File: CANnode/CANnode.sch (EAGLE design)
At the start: 247 parts, among them IC1 ISO1050DUB, IC2 ISO1050DUB, Q1 FDV302P, Q3 FDV302P, U1 LM324PW, U10 FT2232HL, U11 93LC56C-I/SN, U2 TPS70445_PWP_24, U3 LM324PW, U4 LM324PW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

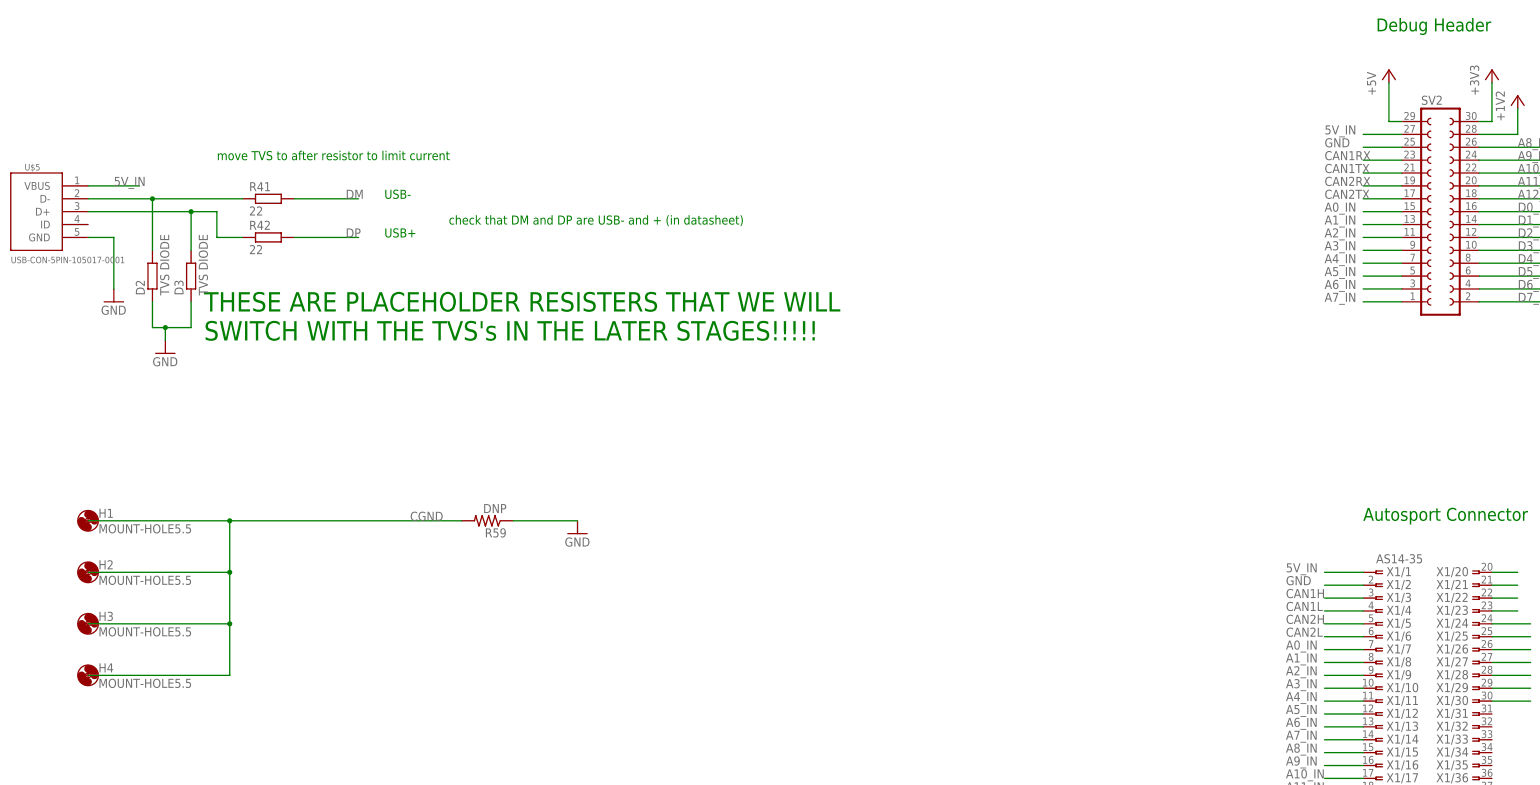
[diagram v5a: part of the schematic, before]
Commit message: Changed mounting holes to big vias. Move the origin of the board.
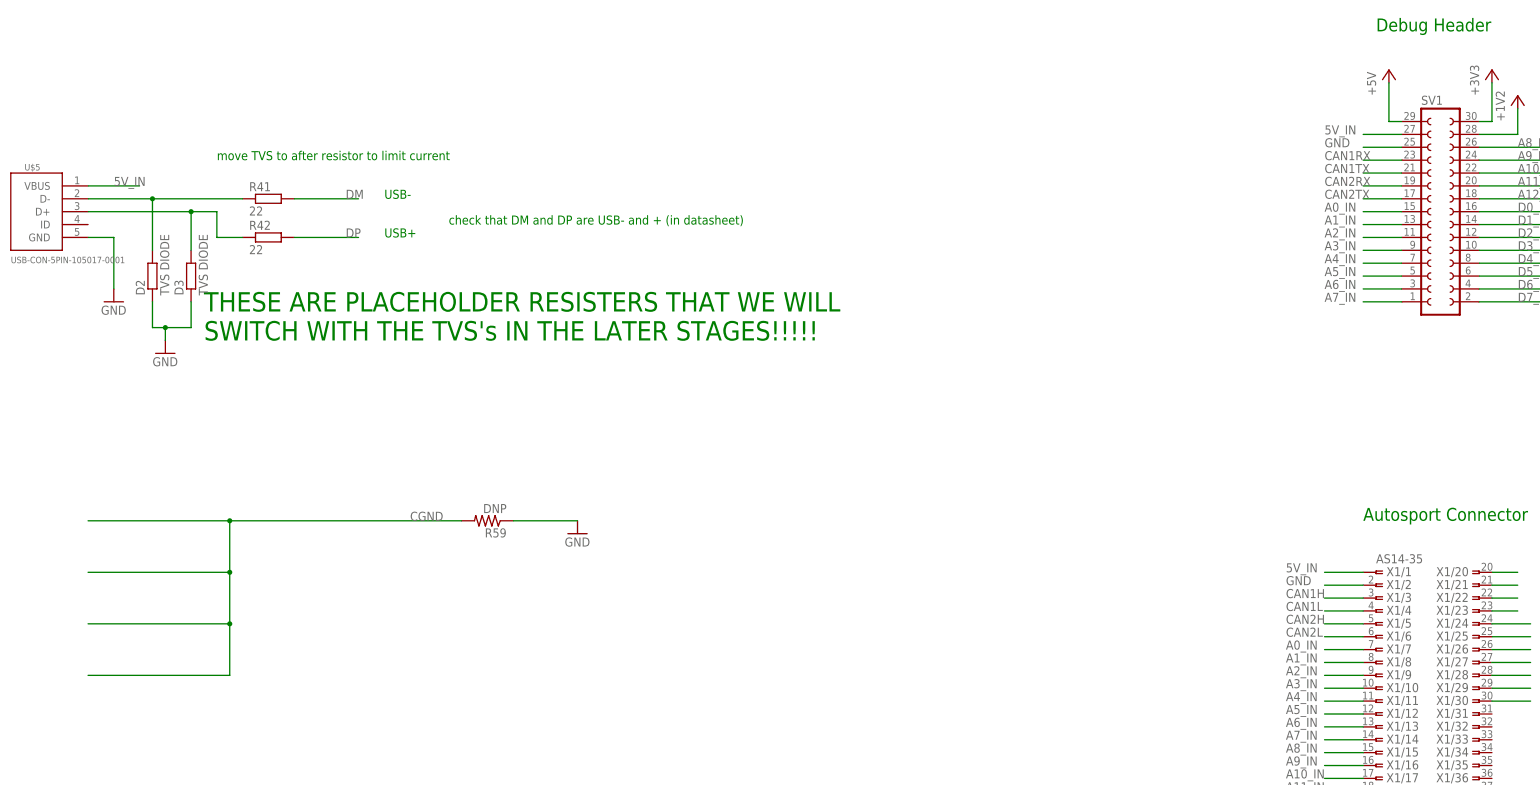
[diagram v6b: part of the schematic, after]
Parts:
- removed H1, H2, H3, H4: MOUNT-HOLE5.5, holes:MOUNT-HOLE5.5
- renumbered SV2 to SV1
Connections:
- net 5V_IN: now also SV1.27
- net A0_IN: now also SV1.15
- net A10_IN: now also SV1.22
- net A11_IN: now also SV1.20
- net A12_IN: now also SV1.18
- net A1_IN: now also SV1.13
- net A2_IN: now also SV1.11
- net A3_IN: now also SV1.9
- net A4_IN: now also SV1.7
- net A5_IN: now also SV1.5
- net A6_IN: now also SV1.3
- net A8_IN: now also SV1.26
- net A9_IN: now also SV1.24
- net CAN1RX: now also SV1.23
- net CAN1TX: now also SV1.21
- net CAN2RX: now also SV1.19
- net CAN2TX: now also SV1.17
- net D0_IN: now also SV1.16
- net D1_IN: now also SV1.14
- net D2_IN: now also SV1.12
- net D3_IN: now also SV1.10
- net D4_IN: now also SV1.8
- net D5_IN: now also SV1.6
- net D6_IN: now also SV1.4
- net GND: now also SV1.25
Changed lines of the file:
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@@
 <part name="GND8" library="supply1" deviceset="GND" device=""/>
 <part name="TP1" library="testpad" deviceset="TPS" device="B1,27"/>
-<part name="SV2" library="con-lsta" deviceset="FE15-2" device=""/>
 <part name="P+4" library="supply1" deviceset="+5V" device=""/>
 <part name="+3V10" library="supply1" deviceset="+3V3" device=""/>
@@
 <part name="D34" library="eagle-ltspice" deviceset="R" device="R0402" value="TVS DIODE"/>
 <part name="D35" library="eagle-ltspice" deviceset="R" device="R0402" value="TVS DIODE"/>
-<part name="H1" library="holes" deviceset="MOUNT-HOLE" device="5.5"/>
-<part name="H2" library="holes" deviceset="MOUNT-HOLE" device="5.5"/>
-<part name="H3" library="holes" deviceset="MOUNT-HOLE" device="5.5"/>
-<part name="H4" library="holes" deviceset="MOUNT-HOLE" device="5.5"/>
 <part name="R59" library="resistor" deviceset="R-US_" device="R0402" value="DNP"/>
 <part name="GND120" library="supply1" deviceset="GND" device=""/>
@@
 <part name="GND123" library="supply1" deviceset="GND" device=""/>
 <part name="F1" library="adafruit" deviceset="PTCFUSE" device="-1206" value="0ZCJ0050AF2E"/>
+<part name="SV1" library="con-lsta" deviceset="FE15-2" device=""/>
 </parts>
 <sheets>
@@
 <instance part="GND8" gate="1" x="50.8" y="-5.08"/>
 <instance part="TP1" gate="G$1" x="116.84" y="-30.48"/>
-<instance part="SV2" gate="1" x="264.16" y="-83.82"/>
 <instance part="P+4" gate="1" x="254" y="-55.88"/>
 <instance part="+3V10" gate="G$1" x="274.32" y="-55.88"/>
@@
 <instance part="D34" gate="G$1" x="657.86" y="-314.96" rot="R90"/>
 <instance part="D35" gate="G$1" x="662.94" y="-360.68" rot="R90"/>
-<instance part="H1" gate="G$1" x="-2.54" y="-144.78"/>
-<instance part="H2" gate="G$1" x="-2.54" y="-154.94"/>
-<instance part="H3" gate="G$1" x="-2.54" y="-165.1"/>
-<instance part="H4" gate="G$1" x="-2.54" y="-175.26"/>
 <instance part="R59" gate="G$1" x="76.2" y="-144.78" rot="R180"/>
 <instance part="GND120" gate="1" x="93.98" y="-147.32"/>
@@
 <instance part="GND123" gate="1" x="58.42" y="-5.08"/>
 <instance part="F1" gate="G$1" x="15.24" y="10.16"/>
+<instance part="SV1" gate="1" x="264.16" y="-83.82"/>
 </instances>
 <busses>
@@
 <pinref part="+3V10" gate="G$1" pin="+3V3"/>
 <wire x1="274.32" y1="-58.42" x2="274.32" y2="-66.04" width="0.1524" layer="91"/>
-<pinref part="SV2" gate="1" pin="30"/>
 <wire x1="274.32" y1="-66.04" x2="271.78" y2="-66.04" width="0.1524" layer="91"/>
+<pinref part="SV1" gate="1" pin="30"/>
 </segment>
 <segment>
@@
 </segment>
 <segment>
-<pinref part="SV2" gate="1" pin="28"/>
 <wire x1="271.78" y1="-68.58" x2="279.4" y2="-68.58" width="0.1524" layer="91"/>
 <wire x1="279.4" y1="-68.58" x2="279.4" y2="-63.5" width="0.1524" layer="91"/>
 <pinref part="U$2" gate="A" pin="+1V2"/>
+<pinref part="SV1" gate="1" pin="28"/>
 </segment>
 </net>
@@
 <wire x1="256.54" y1="-76.2" x2="248.92" y2="-76.2" width="0.1524" layer="91"/>
 <label x="241.3" y="-76.2" size="1.778" layer="95"/>
+<pinref part="SV1" gate="1" pin="21"/>
 </segment>
 </net>
@@
 <wire x1="256.54" y1="-81.28" x2="248.92" y2="-81.28" width="0.1524" layer="91"/>
 <label x="241.3" y="-81.28" size="1.778" layer="95"/>
+<pinref part="SV1" gate="1" pin="17"/>
 </segment>
 </net>
@@
 <wire x1="248.92" y1="-78.74" x2="256.54" y2="-78.74" width="0.1524" layer="91"/>
 <label x="241.3" y="-78.74" size="1.778" layer="95"/>
+<pinref part="SV1" gate="1" pin="19"/>
 </segment>
 </net>
@@
 <wire x1="256.54" y1="-73.66" x2="248.92" y2="-73.66" width="0.1524" layer="91"/>
 <label x="241.3" y="-73.66" size="1.778" layer="95"/>
+<pinref part="SV1" gate="1" pin="23"/>
 </segment>
 </net>
@@
 <wire x1="256.54" y1="-71.12" x2="248.92" y2="-71.12" width="0.1524" layer="91"/>
 <label x="241.3" y="-71.12" size="1.778" layer="95"/>
+<pinref part="SV1" gate="1" pin="25"/>
 </segment>
 <segment>
@@
 <wire x1="256.54" y1="-68.58" x2="248.92" y2="-68.58" width="0.1524" layer="91"/>
 <label x="241.3" y="-68.58" size="1.778" layer="95"/>
+<pinref part="SV1" gate="1" pin="27"/>
 </segment>
 <segment>
@@
 <net name="+5V" class="0">
 <segment>
-<pinref part="SV2" gate="1" pin="29"/>
 <wire x1="256.54" y1="-66.04" x2="254" y2="-66.04" width="0.1524" layer="91"/>
 <pinref part="P+4" gate="1" pin="+5V"/>
 <wire x1="254" y1="-66.04" x2="254" y2="-58.42" width="0.1524" layer="91"/>
+<pinref part="SV1" gate="1" pin="29"/>
 </segment>
 <segment>
@@
 <label x="241.3" y="-83.82" size="1.778" layer="95"/>
 <wire x1="248.92" y1="-83.82" x2="256.54" y2="-83.82" width="0.1524" layer="91"/>
+<pinref part="SV1" gate="1" pin="15"/>
 </segment>
 </net>
@@
 <label x="241.3" y="-93.98" size="1.778" layer="95"/>
 <wire x1="248.92" y1="-93.98" x2="256.54" y2="-93.98" width="0.1524" layer="91"/>
+<pinref part="SV1" gate="1" pin="7"/>
 </segment>
 </net>
@@
 <label x="279.4" y="-71.12" size="1.778" layer="95"/>
 <wire x1="271.78" y1="-71.12" x2="287.02" y2="-71.12" width="0.1524" layer="91"/>
+<pinref part="SV1" gate="1" pin="26"/>
 </segment>
 </net>
@@
 <label x="279.4" y="-81.28" size="1.778" layer="95"/>
 <wire x1="271.78" y1="-81.28" x2="287.02" y2="-81.28" width="0.1524" layer="91"/>
+<pinref part="SV1" gate="1" pin="18"/>
 </segment>
 </net>
@@
 <label x="279.4" y="-83.82" size="1.778" layer="95"/>
 <wire x1="271.78" y1="-83.82" x2="287.02" y2="-83.82" width="0.1524" layer="91"/>
+<pinref part="SV1" gate="1" pin="16"/>
 </segment>
 </net>
@@
 <label x="279.4" y="-93.98" size="1.778" layer="95"/>
 <wire x1="287.02" y1="-93.98" x2="271.78" y2="-93.98" width="0.1524" layer="91"/>
+<pinref part="SV1" gate="1" pin="8"/>
 </segment>
 </net>
@@
 <label x="279.4" y="-96.52" size="1.778" layer="95"/>
 <wire x1="287.02" y1="-96.52" x2="271.78" y2="-96.52" width="0.1524" layer="91"/>
+<pinref part="SV1" gate="1" pin="6"/>
 </segment>
 </net>
@@
 <label x="279.4" y="-86.36" size="1.778" layer="95"/>
 <wire x1="287.02" y1="-86.36" x2="271.78" y2="-86.36" width="0.1524" layer="91"/>
+<pinref part="SV1" gate="1" pin="14"/>
 </segment>
 </net>
@@
 <label x="279.4" y="-73.66" size="1.778" layer="95"/>
 <wire x1="287.02" y1="-73.66" x2="271.78" y2="-73.66" width="0.1524" layer="91"/>
+<pinref part="SV1" gate="1" pin="24"/>
 </segment>
 </net>
@@
 <label x="241.3" y="-96.52" size="1.778" layer="95"/>
 <wire x1="256.54" y1="-96.52" x2="248.92" y2="-96.52" width="0.1524" layer="91"/>
+<pinref part="SV1" gate="1" pin="5"/>
 </segment>
 </net>
@@
 <label x="241.3" y="-86.36" size="1.778" layer="95"/>
 <wire x1="256.54" y1="-86.36" x2="248.92" y2="-86.36" width="0.1524" layer="91"/>
+<pinref part="SV1" gate="1" pin="13"/>
 </segment>
 </net>
@@
 <label x="241.3" y="-88.9" size="1.778" layer="95"/>
 <wire x1="248.92" y1="-88.9" x2="256.54" y2="-88.9" width="0.1524" layer="91"/>
+<pinref part="SV1" gate="1" pin="11"/>
 </segment>
 </net>
@@
 <label x="241.3" y="-91.44" size="1.778" layer="95"/>
 <wire x1="256.54" y1="-91.44" x2="248.92" y2="-91.44" width="0.1524" layer="91"/>
+<pinref part="SV1" gate="1" pin="9"/>
 </segment>
 </net>
@@
 </segment>
 <segment>
-<pinref part="SV2" gate="1" pin="1"/>
 <wire x1="256.54" y1="-101.6" x2="248.92" y2="-101.6" width="0.1524" layer="91"/>
 <label x="241.3" y="-101.6" size="1.778" layer="95"/>
+<pinref part="SV1" gate="1" pin="1"/>
 </segment>
 </net>
@@
 <label x="279.4" y="-78.74" size="1.778" layer="95"/>
 <wire x1="287.02" y1="-78.74" x2="271.78" y2="-78.74" width="0.1524" layer="91"/>
+<pinref part="SV1" gate="1" pin="20"/>
 </segment>
 </net>
@@
 <label x="279.4" y="-91.44" size="1.778" layer="95"/>
 <wire x1="287.02" y1="-91.44" x2="271.78" y2="-91.44" width="0.1524" layer="91"/>
+<pinref part="SV1" gate="1" pin="10"/>
 </segment>
 </net>
@@
 </segment>
 <segment>
-<pinref part="SV2" gate="1" pin="2"/>
 <wire x1="271.78" y1="-101.6" x2="287.02" y2="-101.6" width="0.1524" layer="91"/>
 <label x="279.4" y="-101.6" size="1.778" layer="95"/>
+<pinref part="SV1" gate="1" pin="2"/>
 </segment>
 </net>
@@
 <label x="279.4" y="-99.06" size="1.778" layer="95"/>
 <wire x1="287.02" y1="-99.06" x2="271.78" y2="-99.06" width="0.1524" layer="91"/>
+<pinref part="SV1" gate="1" pin="4"/>
 </segment>
 </net>
@@
 <label x="279.4" y="-88.9" size="1.778" layer="95"/>
 <wire x1="271.78" y1="-88.9" x2="287.02" y2="-88.9" width="0.1524" layer="91"/>
+<pinref part="SV1" gate="1" pin="12"/>
 </segment>
 </net>
@@
 <label x="279.4" y="-76.2" size="1.778" layer="95"/>
 <wire x1="271.78" y1="-76.2" x2="287.02" y2="-76.2" width="0.1524" layer="91"/>
+<pinref part="SV1" gate="1" pin="22"/>
 </segment>
 </net>
@@
 <label x="241.3" y="-99.06" size="1.778" layer="95"/>
 <wire x1="248.92" y1="-99.06" x2="256.54" y2="-99.06" width="0.1524" layer="91"/>
+<pinref part="SV1" gate="1" pin="3"/>
 </segment>
 </net>

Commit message: added connector
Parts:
- added X2: 1751316, con-phoenix-350:1751316
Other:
- note added: "connections: 5V_IN GND 2 AV 2 DI CAN1H CAN1L 5V"
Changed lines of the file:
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@@
 <part name="F1" library="adafruit" deviceset="PTCFUSE" device="-1206" value="0ZCJ0050AF2E"/>
 <part name="SV1" library="con-lsta" deviceset="FE15-2" device=""/>
+<part name="X2" library="con-phoenix-350" deviceset="1751316" device=""/>
 </parts>
 <sheets>
@@
 <text x="55.88" y="-88.9" size="1.778" layer="91">USB+</text>
 <text x="68.58" y="-86.36" size="1.778" layer="91">check that DM and DP are USB- and + (in datasheet)</text>
+<text x="162.56" y="-172.72" size="1.778" layer="91">connections:
+5V_IN
+GND
+2 AV
+2 DI
+CAN1H
+CAN1L
+5V</text>
 </plain>
 <instances>
@@
 <instance part="F1" gate="G$1" x="15.24" y="10.16"/>
 <instance part="SV1" gate="1" x="264.16" y="-83.82"/>
+<instance part="X2" gate="-1" x="182.88" y="-137.16"/>
+<instance part="X2" gate="-2" x="182.88" y="-144.78"/>
+<instance part="X2" gate="-3" x="182.88" y="-152.4"/>
+<instance part="X2" gate="-4" x="182.88" y="-160.02"/>
+<instance part="X2" gate="-5" x="182.88" y="-167.64"/>
+<instance part="X2" gate="-6" x="182.88" y="-175.26"/>
+<instance part="X2" gate="-7" x="182.88" y="-182.88"/>
+<instance part="X2" gate="-8" x="182.88" y="-190.5"/>
+<instance part="X2" gate="-9" x="182.88" y="-198.12"/>
 </instances>
 <busses>
